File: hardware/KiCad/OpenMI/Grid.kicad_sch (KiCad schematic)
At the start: 19 parts, among them K2 RT424012, Q6 BSS123L, U6 CAP005DG

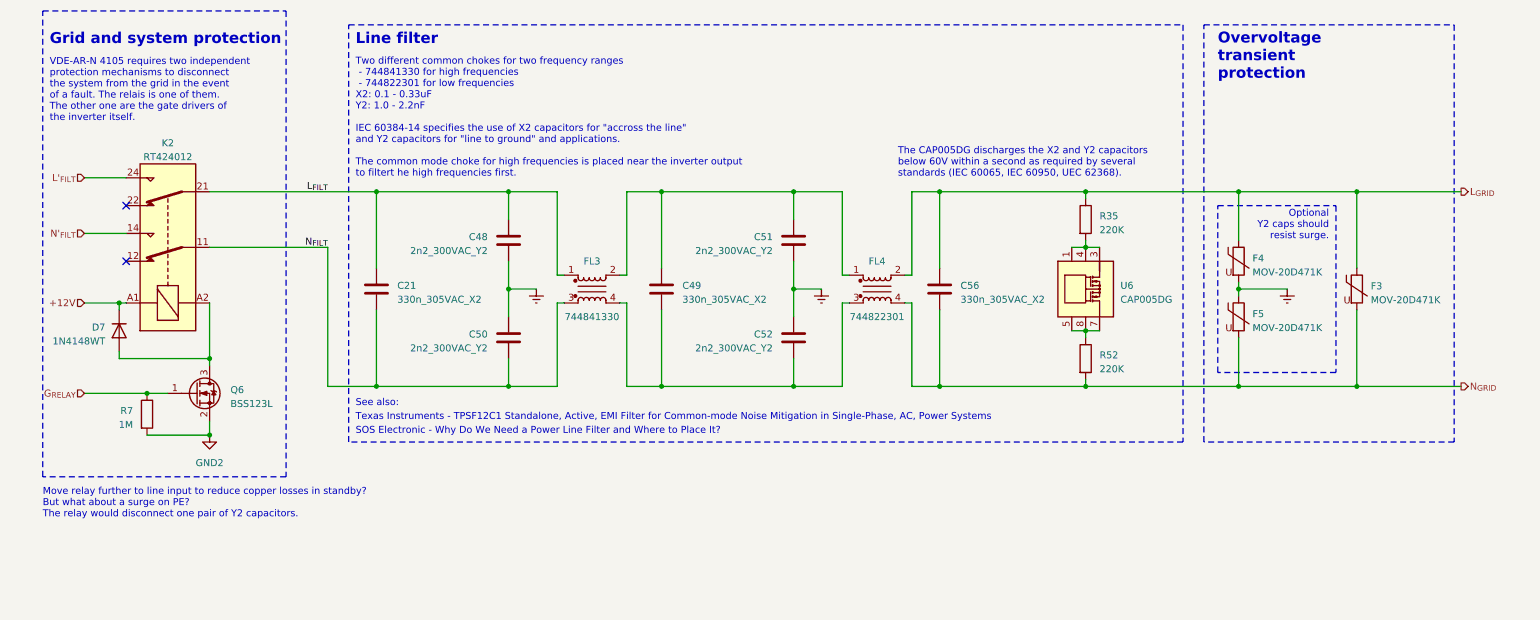
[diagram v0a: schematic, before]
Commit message: feat: Adds grid current sensing using a hall effect sensor.
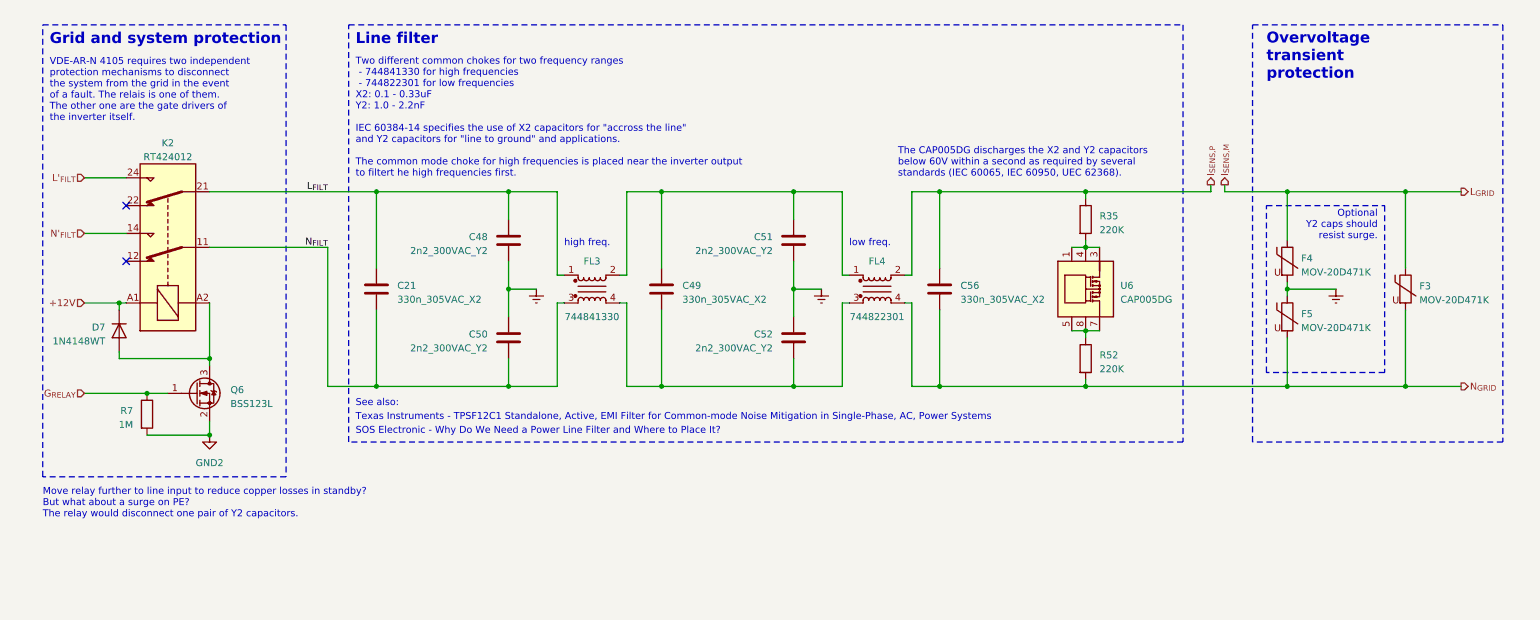
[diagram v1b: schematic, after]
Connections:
- net L_{GRID} renamed I_{SENS,P}
- net I_{SENS,P}: no longer F3.1, F4.1
- new net I_{SENS,M}: F3.1, F4.1
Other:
- note added: "high freq."
- note added: "low freq."
- moved on the sheet: F3, F4, F5

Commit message: docs(hw): Adds explanation of why Y2 capacitors do not need overvoltage protection.
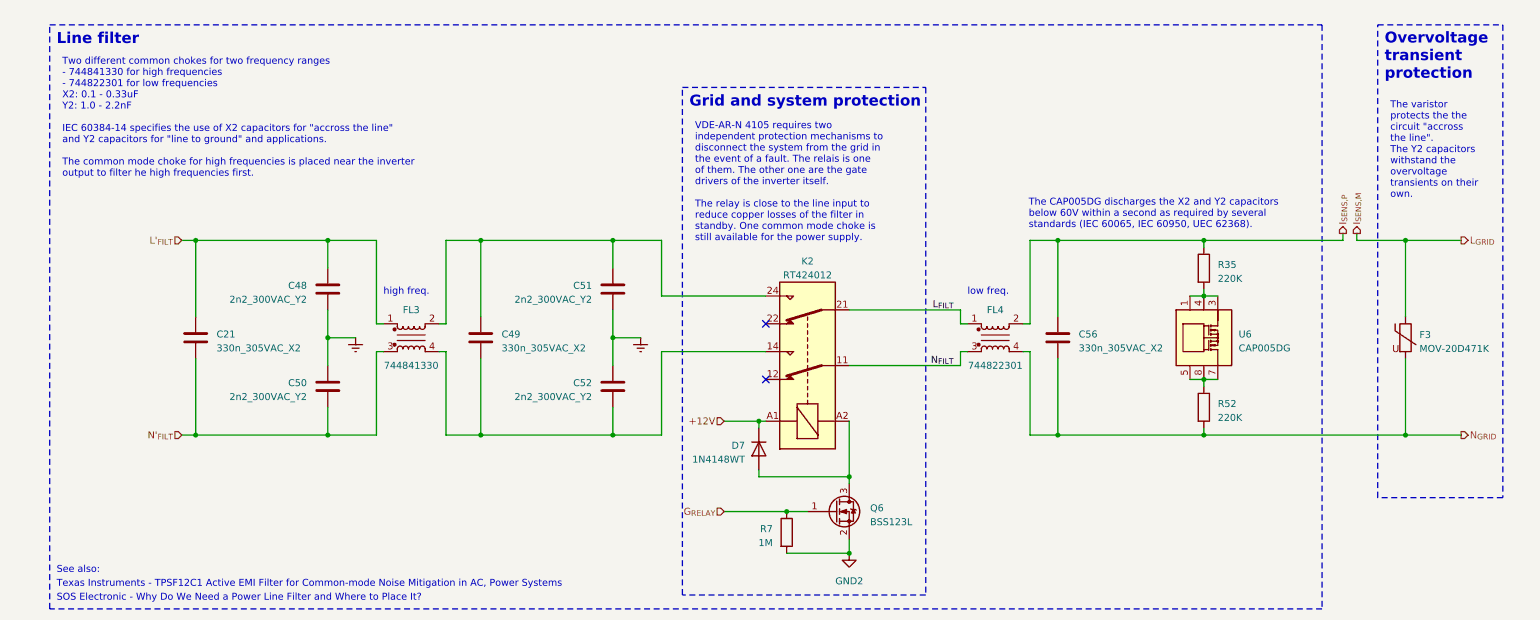
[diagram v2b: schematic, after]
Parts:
- removed F4, F5: MOV-20D471K, Varistor:RV_Disc_D21.5mm_W5.8mm_P10mm, symbol _Varistor:MOV-20D471K
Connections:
- net L'_{FILT}: now also C21.1, C48.1, FL3.1; no longer K2.24
- net L_{FILT}: now also FL4.1; no longer C21.1, C48.1, FL3.1
- net N'_{FILT}: now also C21.2, C50.2, FL3.3; no longer K2.14
- net N_{FILT}: now also FL4.3; no longer C21.2, C50.2, FL3.3
- net at C49.1, C51.1, FL3.2: now also K2.24; no longer FL4.1
- net at C49.2, C52.2, FL3.4: now also K2.14; no longer FL4.3
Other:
- note added: "Texas Instruments - TPSF12C1 Active EMI Filter for Common-mode Noise Mitigation in AC, Power Systems"
- note removed: "Move relay further to line input to reduce copper losses in standby? But what about a surge on PE? The relay would disconnect one pair of Y2 capacitors."
- note removed: "Optional Y2 caps should resist surge."
- note removed: "Texas Instruments - TPSF12C1 Standalone, Active, EMI Filter for Common-mode Noise Mitigation in Single-Phase, AC, Power Systems"
- note removed: "The CAP005DG discharges the X2 and Y2 capacitors below 60V within a second as required by several standards (IEC 60065, IEC 60950, UEC 62368)."
- note removed: "Two different common chokes for two frequency ranges - 744841330 for high frequencies - 744822301 for low frequencies X2: 0.1 - 0.33uF Y2: 1.0 - 2.2nF IEC 60384-14 specifies the use of X2 capacitors for "accross the line" and Y2 capacitors for "line to ground" and applications. The common mode choke for high frequencies is placed near the inverter output to filtert he high frequencies first."
- note removed: "VDE-AR-N 4105 requires two independent protection mechanisms to disconnect the system from the grid in the event of a fault. The relais is one of them. The other one are the gate drivers of the inverter itself."
- moved on the sheet: C21, C48, C49, C50, C51, C52, C56, D7, F3, FL3, FL4, K2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
